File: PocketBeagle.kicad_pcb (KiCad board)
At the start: 4 copper layers, 55 x 35 mm, 32 parts, among them J1 Conn_01x08_Male, J10 Conn_01x04_Male, J11 Conn_01x04_Male, J12 Conn_01x04_Male, J13 Conn_01x04_Male, J14 Conn_01x04_Male, J15 Conn_01x04_Male, J16 Conn_01x04_Male, J17 Conn_01x02_Male, J18 Conn_01x02_Male, J19 Conn_01x01_Male, J2 Conn_01x04_Male, J20 Conn_01x01_Male, J21 Conn_01x04_Male, J22 Conn_01x04_Male, J23 Conn_01x02_Male, J24 Conn_01x02_Male, J25 Conn_01x01_Male, J26 Conn_01x01_Male, J27 Conn_01x04_Male, J28 Conn_01x04_Male, J29 Conn_01x01_Male, J3 Conn_01x04_Male, J30 Conn_01x01_Male, J31 Conn_01x01_Male, J32 Conn_01x01_Male, J4 Conn_01x08_Male, J5 Conn_01x04_Male, J6 Conn_01x04_Male, J7 Conn_01x04_Male, J8 Conn_01x04_Male, J9 Conn_01x04_Male

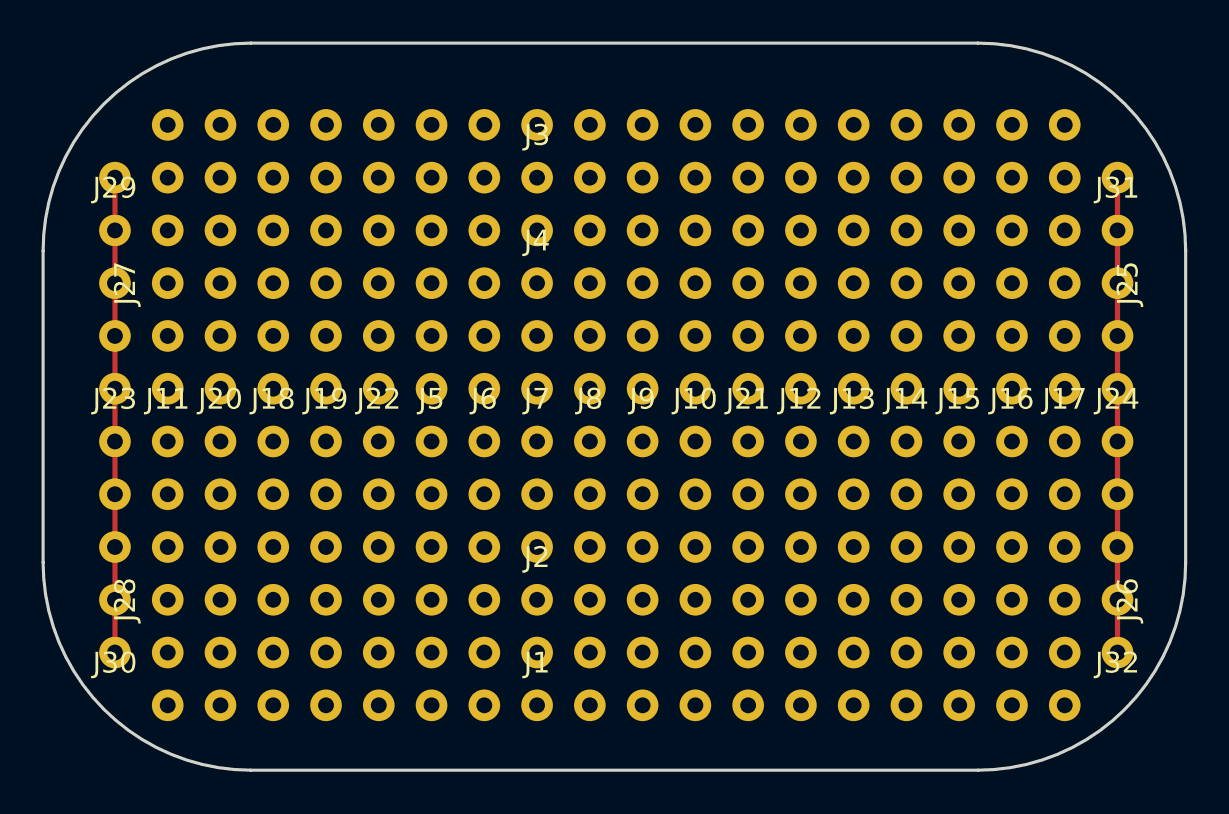
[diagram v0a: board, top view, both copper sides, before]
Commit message: Correct misalignment and delete unnecessary files. 位置ずれの修正と、不要なファイルの削除。
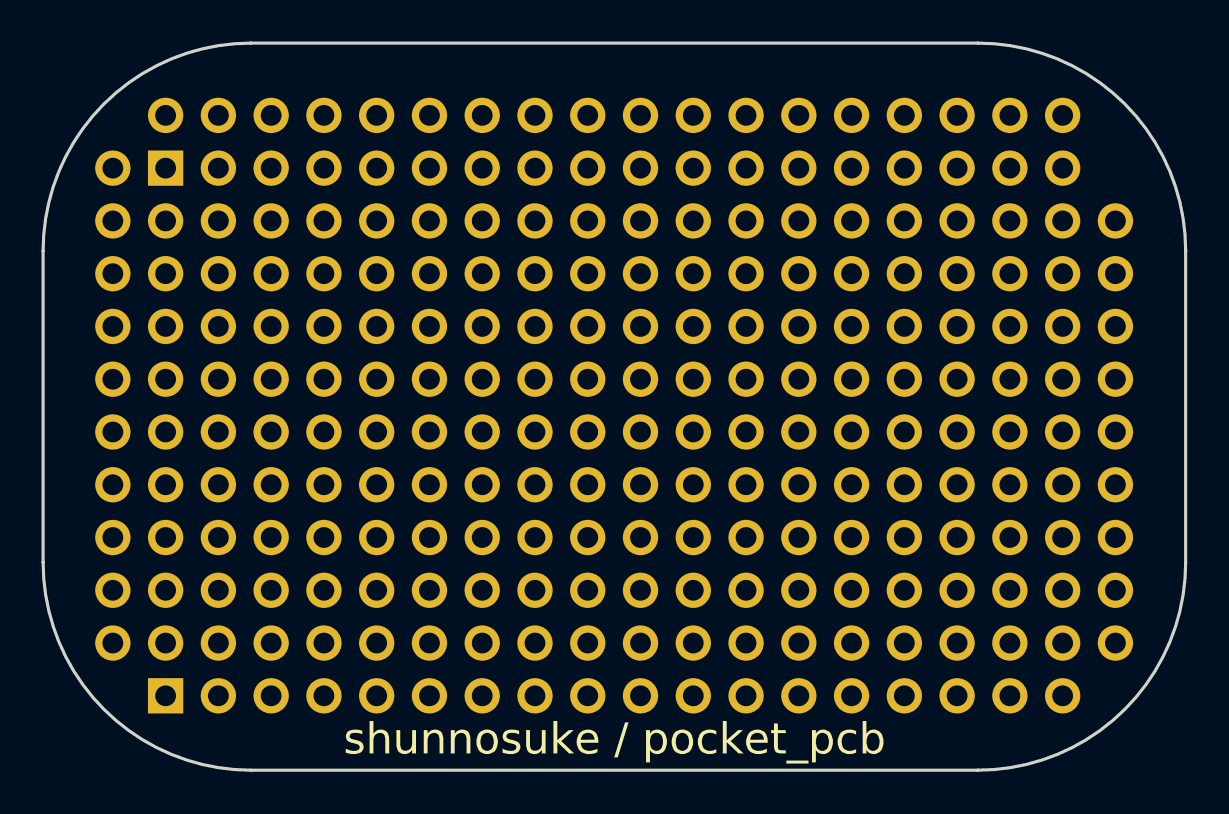
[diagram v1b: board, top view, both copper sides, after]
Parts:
- removed J25, J26: Conn_01x01_Male, pocketbeagle:j 2
- removed J27, J28: Conn_01x04_Male, pocketbeagle:j 2
- removed J29, J30, J31, J32: Conn_01x01_Male, pocketbeagle:j 1
- J1, J4: value Conn_01x08_Male -> Conn_01x18_Male; footprint pocketbeagle:端子 -> Connector_PinHeader_2.54mm:PinHeader_1x18_P2.54mm_Vertical
- J10, J11, J12, J13, J14, J15, J16, J21, J22, J7, J8, J9: value Conn_01x04_Male -> Conn_01x08_Male; footprint pocketbeagle:yb -> Connector_PinHeader_2.54mm:PinHeader_1x08_P2.54mm_Vertical
- J17, J18, J23, J24: value Conn_01x02_Male -> Conn_01x08_Male; footprint pocketbeagle:yb -> Connector_PinHeader_2.54mm:PinHeader_1x08_P2.54mm_Vertical
- J19, J20: value Conn_01x01_Male -> Conn_01x08_Male; footprint pocketbeagle:yb -> Connector_PinHeader_2.54mm:PinHeader_1x08_P2.54mm_Vertical
- J2, J3: value Conn_01x04_Male -> Conn_01x18_Male; footprint pocketbeagle:端子 -> Connector_PinHeader_2.54mm:PinHeader_1x18_P2.54mm_Vertical
- J5, J6: value Conn_01x04_Male -> Conn_01x10_Male; footprint pocketbeagle:yb -> Connector_PinHeader_2.54mm:PinHeader_1x10_P2.54mm_Vertical
- moved J23 43.8 mm to (167.5, 96.1)
- moved J6 32.2 mm to (172.6, 93.5)
- moved J20 31.4 mm to (159.9, 96.1)
- moved J22 29.0 mm to (165.0, 96.1)
- moved J18 24.1 mm to (154.8, 96.1)
- moved J19 24.1 mm to (157.4, 96.1)
- moved J13 19.6 mm to (142.1, 96.1)
- moved J17 19.6 mm to (152.3, 96.1)
- moved J9 19.6 mm to (132.0, 96.1)
- moved J7 19.6 mm to (126.9, 96.1)
- moved J10 19.6 mm to (134.5, 96.1)
- moved J12 19.6 mm to (139.6, 96.1)
- moved J14 19.6 mm to (144.7, 96.1)
- moved J15 19.6 mm to (147.2, 96.1)
- moved J16 19.6 mm to (149.8, 96.1)
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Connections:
- J1 pad 10: (no net) -> Net-(J1-Pad10)
- J1 pad 11: (no net) -> Net-(J1-Pad11)
- J1 pad 12: (no net) -> Net-(J1-Pad12)
- J1 pad 13: (no net) -> Net-(J1-Pad13)
- J1 pad 14: (no net) -> Net-(J1-Pad14)
- J1 pad 15: (no net) -> Net-(J1-Pad15)
- J1 pad 16: (no net) -> Net-(J1-Pad16)
- J1 pad 17: (no net) -> Net-(J1-Pad17)
- J1 pad 18: (no net) -> Net-(J1-Pad18)
- J1 pad 9: (no net) -> Net-(J1-Pad9)
- J16 pad 2: Net-(J16-Pad1) -> Net-(J16-Pad2)
- J16 pad 3: Net-(J16-Pad1) -> Net-(J16-Pad3)
- J16 pad 4: Net-(J16-Pad1) -> Net-(J16-Pad4)
- J17 pad 1: Net-(J16-Pad1) -> Net-(J17-Pad1)
- J17 pad 2: Net-(J16-Pad1) -> Net-(J17-Pad2)
- J17 pad 3: (no net) -> Net-(J17-Pad3)
- J17 pad 4: (no net) -> Net-(J17-Pad4)
- J18 pad 1: Net-(J16-Pad1) -> Net-(J18-Pad1)
- J18 pad 2: Net-(J16-Pad1) -> Net-(J18-Pad2)
- J18 pad 3: (no net) -> Net-(J18-Pad3)
- J18 pad 4: (no net) -> Net-(J18-Pad4)
- J19 pad 1: Net-(J16-Pad1) -> Net-(J19-Pad1)
- J19 pad 2: (no net) -> Net-(J19-Pad2)
- J19 pad 3: (no net) -> Net-(J19-Pad3)
- J19 pad 4: (no net) -> Net-(J19-Pad4)
- J2 pad 10: (no net) -> Net-(J2-Pad10)
- J2 pad 11: (no net) -> Net-(J2-Pad11)
- J2 pad 12: (no net) -> Net-(J2-Pad12)
- J2 pad 13: (no net) -> Net-(J2-Pad13)
- J2 pad 14: (no net) -> Net-(J2-Pad14)
- J2 pad 15: (no net) -> Net-(J2-Pad15)
- J2 pad 16: (no net) -> Net-(J2-Pad16)
- J2 pad 17: (no net) -> Net-(J2-Pad17)
- J2 pad 18: (no net) -> Net-(J2-Pad18)
- J2 pad 5: (no net) -> Net-(J2-Pad5)
- J2 pad 6: (no net) -> Net-(J2-Pad6)
- J2 pad 7: (no net) -> Net-(J2-Pad7)
- J2 pad 8: (no net) -> Net-(J2-Pad8)
- J2 pad 9: (no net) -> Net-(J2-Pad9)
- J20 pad 1: Net-(J16-Pad1) -> Net-(J20-Pad1)
- J20 pad 2: (no net) -> Net-(J20-Pad2)
- J20 pad 3: (no net) -> Net-(J20-Pad3)
- J20 pad 4: (no net) -> Net-(J20-Pad4)
- J22 pad 2: Net-(J22-Pad1) -> Net-(J22-Pad2)
- J22 pad 3: Net-(J22-Pad1) -> Net-(J22-Pad3)
- J22 pad 4: Net-(J22-Pad1) -> Net-(J22-Pad4)
- J23 pad 1: Net-(J22-Pad1) -> Net-(J23-Pad1)
- J23 pad 2: Net-(J22-Pad1) -> Net-(J23-Pad2)
- J23 pad 3: (no net) -> Net-(J23-Pad3)
- J23 pad 4: (no net) -> Net-(J23-Pad4)
- J24 pad 1: Net-(J22-Pad1) -> Net-(J24-Pad1)
- J24 pad 2: Net-(J22-Pad1) -> Net-(J24-Pad2)
- J24 pad 3: (no net) -> Net-(J24-Pad3)
- J24 pad 4: (no net) -> Net-(J24-Pad4)
- J3 pad 11: (no net) -> Net-(J3-Pad11)
- J3 pad 13: (no net) -> Net-(J3-Pad13)
- J3 pad 15: (no net) -> Net-(J3-Pad15)
- J3 pad 17: (no net) -> Net-(J3-Pad17)
- J3 pad 5: (no net) -> Net-(J3-Pad5)
- J3 pad 7: (no net) -> Net-(J3-Pad7)
- J3 pad 9: (no net) -> Net-(J3-Pad9)
- J4 pad 10: (no net) -> Net-(J4-Pad10)
- J4 pad 11: (no net) -> Net-(J4-Pad11)
- J4 pad 12: (no net) -> Net-(J4-Pad12)
- J4 pad 13: (no net) -> Net-(J4-Pad13)
- J4 pad 14: (no net) -> Net-(J4-Pad14)
- J4 pad 15: (no net) -> Net-(J4-Pad15)
- J4 pad 16: (no net) -> Net-(J4-Pad16)
- J4 pad 17: (no net) -> Net-(J4-Pad17)
- J4 pad 18: (no net) -> Net-(J4-Pad18)
- J4 pad 9: (no net) -> Net-(J4-Pad9)
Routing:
- net Net-(J24-Pad1): track 22.9 -> 0.00 mm
- net Net-(J23-Pad1): track 22.9 -> 0.00 mm
- removed copper zone on DigitalGND, net GND
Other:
- board text added: "75 Mils back--> Try to move back 75 Mils <---"
- board text added: "FillOverPAD:CGND:19:484"
- board text added: "FillOverPAD:CGND:19:532"
- board text added: "FillOverPAD:CGND:459:484"
- board text added: "FillOverPAD:CGND:460:484"
- board text added: "FillOverPAD:CGND:461:484"
- board text added: "FillOverPAD:CGND:462:484"
- board text added: "FillOverPAD:CGND:463:484"
- board text added: "FillOverPAD:CGND:464:484"
- board text added: "FillOverPAD:CGND:479:484"
- board text added: "FillOverPAD:CGND:480:484"
- board text added: "FillOverPAD:CGND:481:484"
- board text added: "FillOverPAD:CGND:482:484"
- board text added: "FillOverPAD:CGND:507:532"
- board text added: "FillOverPAD:CGND:508:532"
- board text added: "FillOverPAD:CGND:509:532"
- board text added: "FillOverPAD:CGND:510:532"
- board text added: "FillOverPAD:CGND:511:532"
- board text added: "FillOverPAD:CGND:512:532"
- board text added: "FillOverPAD:CGND:527:532"
- board text added: "FillOverPAD:CGND:528:532"
- board text added: "FillOverPAD:CGND:529:532"
- board text added: "FillOverPAD:CGND:530:532"
- board text added: "FillOverPAD:GND:102:484"
- board text added: "FillOverPAD:GND:102:532"
- board text added: "FillOverPAD:GND:106:484"
- board text added: "FillOverPAD:GND:106:532"
- board text added: "FillOverPAD:GND:10:484"
- board text added: "FillOverPAD:GND:10:532"
- board text added: "FillOverPAD:GND:112:484"
- board text added: "FillOverPAD:GND:112:532"
- board text added: "FillOverPAD:GND:113:484"
- board text added: "FillOverPAD:GND:113:532"
- board text added: "FillOverPAD:GND:114:484"
- board text added: "FillOverPAD:GND:114:532"
- board text added: "FillOverPAD:GND:115:484"
- board text added: "FillOverPAD:GND:115:532"
- board text added: "FillOverPAD:GND:120:484"
- board text added: "FillOverPAD:GND:120:532"
- board text added: "FillOverPAD:GND:123:484"
- board text added: "FillOverPAD:GND:123:532"
- board text added: "FillOverPAD:GND:128:484"
- board text added: "FillOverPAD:GND:128:532"
- board text added: "FillOverPAD:GND:129:484"
- board text added: "FillOverPAD:GND:129:532"
- board text added: "FillOverPAD:GND:12:484"
- board text added: "FillOverPAD:GND:12:532"
- board text added: "FillOverPAD:GND:131:484"
- board text added: "FillOverPAD:GND:131:532"
- board text added: "FillOverPAD:GND:136:484"
- board text added: "FillOverPAD:GND:136:532"
- board text added: "FillOverPAD:GND:137:484"
- board text added: "FillOverPAD:GND:137:532"
- board text added: "FillOverPAD:GND:138:484"
- board text added: "FillOverPAD:GND:138:532"
- board text added: "FillOverPAD:GND:139:484"
- board text added: "FillOverPAD:GND:139:532"
- board text added: "FillOverPAD:GND:145:484"
- board text added: "FillOverPAD:GND:145:532"
- board text added: "FillOverPAD:GND:146:484"
- board text added: "FillOverPAD:GND:146:532"
- board text added: "FillOverPAD:GND:147:484"
- board text added: "FillOverPAD:GND:147:532"
- board text added: "FillOverPAD:GND:148:484"
- board text added: "FillOverPAD:GND:148:532"
- board text added: "FillOverPAD:GND:149:484"
- board text added: "FillOverPAD:GND:149:532"
- board text added: "FillOverPAD:GND:150:484"
- board text added: "FillOverPAD:GND:150:532"
- board text added: "FillOverPAD:GND:172:484"
- board text added: "FillOverPAD:GND:172:532"
- board text added: "FillOverPAD:GND:20:484"
- board text added: "FillOverPAD:GND:20:532"
- board text added: "FillOverPAD:GND:238:484"
- board text added: "FillOverPAD:GND:238:532"
- board text added: "FillOverPAD:GND:239:484"
- board text added: "FillOverPAD:GND:239:532"
- board text added: "FillOverPAD:GND:251:484"
- board text added: "FillOverPAD:GND:251:532"
- board text added: "FillOverPAD:GND:252:484"
- board text added: "FillOverPAD:GND:252:532"
- board text added: "FillOverPAD:GND:253:484"
- board text added: "FillOverPAD:GND:253:532"
- board text added: "FillOverPAD:GND:254:484"
- board text added: "FillOverPAD:GND:254:532"
- board text added: "FillOverPAD:GND:255:484"
- board text added: "FillOverPAD:GND:255:532"
- board text added: "FillOverPAD:GND:256:484"
- board text added: "FillOverPAD:GND:256:532"
- board text added: "FillOverPAD:GND:257:484"
- board text added: "FillOverPAD:GND:257:532"
- board text added: "FillOverPAD:GND:258:484"
- board text added: "FillOverPAD:GND:258:532"
- board text added: "FillOverPAD:GND:267:484"
- board text added: "FillOverPAD:GND:267:532"
- board text added: "FillOverPAD:GND:274:484"
- board text added: "FillOverPAD:GND:274:532"
- board text added: "FillOverPAD:GND:283:484"
- board text added: "FillOverPAD:GND:283:532"
- board text added: "FillOverPAD:GND:290:484"
- board text added: "FillOverPAD:GND:290:532"
- board text added: "FillOverPAD:GND:298:484"
- board text added: "FillOverPAD:GND:298:532"
- board text added: "FillOverPAD:GND:299:484"
- board text added: "FillOverPAD:GND:299:532"
- board text added: "FillOverPAD:GND:2:484"
- board text added: "FillOverPAD:GND:2:532"
- board text added: "FillOverPAD:GND:306:484"
- board text added: "FillOverPAD:GND:306:532"
- board text added: "FillOverPAD:GND:307:484"
- board text added: "FillOverPAD:GND:307:532"
- board text added: "FillOverPAD:GND:314:484"
- board text added: "FillOverPAD:GND:314:532"
- board text added: "FillOverPAD:GND:315:484"
- board text added: "FillOverPAD:GND:315:532"
- board text added: "FillOverPAD:GND:322:484"
- board text added: "FillOverPAD:GND:322:532"
- board text added: "FillOverPAD:GND:323:484"
- board text added: "FillOverPAD:GND:323:532"
- board text added: "FillOverPAD:GND:331:484"
- board text added: "FillOverPAD:GND:331:532"
- board text added: "FillOverPAD:GND:338:484"
- board text added: "FillOverPAD:GND:338:532"
- board text added: "FillOverPAD:GND:347:484"
- board text added: "FillOverPAD:GND:347:532"
- board text added: "FillOverPAD:GND:354:484"
- board text added: "FillOverPAD:GND:354:532"
- board text added: "FillOverPAD:GND:363:484"
- board text added: "FillOverPAD:GND:363:532"
- board text added: "FillOverPAD:GND:364:484"
- board text added: "FillOverPAD:GND:364:532"
- board text added: "FillOverPAD:GND:365:484"
- board text added: "FillOverPAD:GND:365:532"
- board text added: "FillOverPAD:GND:366:484"
- board text added: "FillOverPAD:GND:366:532"
- board text added: "FillOverPAD:GND:367:484"
- board text added: "FillOverPAD:GND:367:532"
- board text added: "FillOverPAD:GND:368:484"
- board text added: "FillOverPAD:GND:368:532"
- board text added: "FillOverPAD:GND:369:484"
- board text added: "FillOverPAD:GND:369:532"
- board text added: "FillOverPAD:GND:370:484"
- board text added: "FillOverPAD:GND:370:532"
- board text added: "FillOverPAD:GND:382:484"
- board text added: "FillOverPAD:GND:382:532"
- board text added: "FillOverPAD:GND:383:484"
- board text added: "FillOverPAD:GND:383:532"
- board text added: "FillOverPAD:GND:441:484"
- board text added: "FillOverPAD:GND:441:532"
- board text added: "FillOverPAD:GND:447:484"
- board text added: "FillOverPAD:GND:447:532"
- board text added: "FillOverPAD:GND:467:484"
- board text added: "FillOverPAD:GND:475:484"
- board text added: "FillOverPAD:GND:515:532"
- board text added: "FillOverPAD:GND:523:532"
- board text added: "FillOverPAD:GND:8:484"
- board text added: "FillOverPAD:GND:8:532"
- board text added: "FillOverPAD:GND:96:484"
- board text added: "FillOverPAD:GND:96:532"
- board text added: "FillOverPAD:GND:97:484"
- board text added: "FillOverPAD:GND:97:532"
- board text added: "FillOverPAD:SYS_5V:332:484"
- board text added: "FillOverPAD:SYS_5V:332:532"
- board text added: "FillOverPAD:SYS_5V:333:484"
- board text added: "FillOverPAD:SYS_5V:333:532"
- board text added: "FillOverPAD:SYS_5V:348:484"
- board text added: "FillOverPAD:SYS_5V:348:532"
- board text added: "FillOverPAD:SYS_5V:349:484"
- board text added: "FillOverPAD:SYS_5V:349:532"
- board text added: "FillOverPAD:USB_DC:18:484"
- board text added: "FillOverPAD:USB_DC:18:532"
- board text added: "FillOverPAD:USB_DC:326:484"
- board text added: "FillOverPAD:USB_DC:326:532"
- board text added: "FillOverPAD:USB_DC:399:484"
- board text added: "FillOverPAD:USB_DC:399:532"
- board text added: "FillOverPAD:USB_DC:415:484"
- board text added: "FillOverPAD:USB_DC:415:532"
- board text added: "FillOverPAD:USB_DC:431:484"
- board text added: "FillOverPAD:USB_DC:431:532"
- board text added: "FillOverPAD:USB_DC:449:484"
- board text added: "FillOverPAD:USB_DC:449:532"
- board text added: "FillOverPAD:USB_DC:7:484"
- board text added: "FillOverPAD:USB_DC:7:532"
- board text added: "FillOverPAD:VBUS.RAW:17:484"
- board text added: "FillOverPAD:VBUS.RAW:17:532"
- board text added: "FillOverPAD:VBUS.RAW:469:484"
- board text added: "FillOverPAD:VBUS.RAW:517:532"
- board text added: "FillOverPAD:VDD_1V8:272:484"
- board text added: "FillOverPAD:VDD_1V8:272:532"
- board text added: "FillOverPAD:VDD_1V8:288:484"
- board text added: "FillOverPAD:VDD_1V8:288:532"
- board text added: "FillOverPAD:VDD_1V8:304:484"
- board text added: "FillOverPAD:VDD_1V8:304:532"
- board text added: "FillOverPAD:VDD_1V8:305:484"
- board text added: "FillOverPAD:VDD_1V8:305:532"
- board text added: "FillOverPAD:VDD_1V8:320:484"
- board text added: "FillOverPAD:VDD_1V8:320:532"
- board text added: "FillOverPAD:VDD_1V8:321:484"
- board text added: "FillOverPAD:VDD_1V8:321:532"
- board text added: "FillOverPAD:VDD_1V8:336:484"
- board text added: "FillOverPAD:VDD_1V8:336:532"
- board text added: "FillOverPAD:VDD_1V8:352:484"
- board text added: "FillOverPAD:VDD_1V8:352:532"
- board text added: "FillOverPAD:VDD_3V3A:270:484"
- board text added: "FillOverPAD:VDD_3V3A:270:532"
- board text added: "FillOverPAD:VDD_3V3A:271:484"
- board text added: "FillOverPAD:VDD_3V3A:271:532"
- board text added: "FillOverPAD:VDD_3V3A:286:484"
- board text added: "FillOverPAD:VDD_3V3A:286:532"
- board text added: "FillOverPAD:VDD_3V3A:287:484"
- board text added: "FillOverPAD:VDD_3V3A:287:532"
- board text added: "FillOverPAD:VDD_3V3A:301:484"
- board text added: "FillOverPAD:VDD_3V3A:301:532"
- board text added: "FillOverPAD:VDD_3V3A:302:484"
- board text added: "FillOverPAD:VDD_3V3A:302:532"
- board text added: "FillOverPAD:VDD_3V3A:303:484"
- board text added: "FillOverPAD:VDD_3V3A:303:532"
- board text added: "FillOverPAD:VDD_3V3A:317:484"
- board text added: "FillOverPAD:VDD_3V3A:317:532"
- board text added: "FillOverPAD:VDD_3V3A:318:484"
- board text added: "FillOverPAD:VDD_3V3A:318:532"
- board text added: "FillOverPAD:VDD_3V3A:319:484"
- board text added: "FillOverPAD:VDD_3V3A:319:532"
- board text added: "FillOverPAD:VDD_3V3A:334:484"
- board text added: "FillOverPAD:VDD_3V3A:334:532"
- board text added: "FillOverPAD:VDD_3V3A:335:484"
- board text added: "FillOverPAD:VDD_3V3A:335:532"
- board text added: "FillOverPAD:VDD_3V3A:350:484"
- board text added: "FillOverPAD:VDD_3V3A:350:532"
- board text added: "FillOverPAD:VDD_3V3A:351:484"
- board text added: "FillOverPAD:VDD_3V3A:351:532"
- board text added: "FillOverPAD:VDD_3V3AUX:100:484"
- board text added: "FillOverPAD:VDD_3V3AUX:100:532"
- board text added: "FillOverPAD:VDD_3V3AUX:273:484"
- board text added: "FillOverPAD:VDD_3V3AUX:273:532"
- board text added: "FillOverPAD:VDD_3V3AUX:289:484"
- board text added: "FillOverPAD:VDD_3V3AUX:289:532"
- board text added: "FillOverPAD:VDD_3V3B:11:484"
- board text added: "FillOverPAD:VDD_3V3B:11:532"
- board text added: "FillOverPAD:VDD_3V3B:130:484"
- board text added: "FillOverPAD:VDD_3V3B:130:532"
- board text added: "FillOverPAD:VDD_3V3B:144:484"
- board text added: "FillOverPAD:VDD_3V3B:144:532"
- board text added: "FillOverPAD:VDD_3V3B:151:484"
- board text added: "FillOverPAD:VDD_3V3B:151:532"
- board text added: "FillOverPAD:VDD_3V3B:160:484"
- board text added: "FillOverPAD:VDD_3V3B:160:532"
- board text added: "FillOverPAD:VDD_3V3B:161:484"
- board text added: "FillOverPAD:VDD_3V3B:161:532"
- board text added: "FillOverPAD:VDD_3V3B:162:484"
- board text added: "FillOverPAD:VDD_3V3B:162:532"
- board text added: "FillOverPAD:VDD_3V3B:163:484"
- board text added: "FillOverPAD:VDD_3V3B:163:532"
- board text added: "FillOverPAD:VDD_3V3B:165:484"
- board text added: "FillOverPAD:VDD_3V3B:165:532"
- board text added: "FillOverPAD:VDD_3V3B:166:484"
- board text added: "FillOverPAD:VDD_3V3B:166:532"
- board text added: "FillOverPAD:VDD_3V3B:167:484"
- board text added: "FillOverPAD:VDD_3V3B:167:532"
- board text added: "FillOverPAD:VDD_3V3B:268:484"
- board text added: "FillOverPAD:VDD_3V3B:268:532"
- board text added: "FillOverPAD:VDD_3V3B:269:484"
- board text added: "FillOverPAD:VDD_3V3B:269:532"
- board text added: "FillOverPAD:VDD_3V3B:284:484"
- board text added: "FillOverPAD:VDD_3V3B:284:532"
- board text added: "FillOverPAD:VDD_3V3B:285:484"
- board text added: "FillOverPAD:VDD_3V3B:285:532"
- board text added: "FillOverPAD:VDD_3V3B:473:484"
- board text added: "FillOverPAD:VDD_3V3B:521:532"
- board text added: "FillOverPAD:VDD_3V3B:9:484"
- board text added: "FillOverPAD:VDD_3V3B:9:532"
- board text added: "FillOverPAD:VDD_5V:400:484"
- board text added: "FillOverPAD:VDD_5V:400:532"
- board text added: "FillOverPAD:VDD_5V:416:484"
- board text added: "FillOverPAD:VDD_5V:416:532"
- board text added: "FillOverPAD:VDD_5V:432:484"
- board text added: "FillOverPAD:VDD_5V:432:532"
- board text added: "FillOverPAD:VDD_RTC:1:484"
- board text added: "FillOverPAD:VDD_RTC:1:532"
- board text added: "FillOverPAD:VDD_RTC:337:484"
- board text added: "FillOverPAD:VDD_RTC:337:532"
- board text added: "FillOverPAD:VDD_RTC:353:484"
- board text added: "FillOverPAD:VDD_RTC:353:532"
- board text added: "FillOverPAD:VDD_RTC:443:484"
- board text added: "FillOverPAD:VDD_RTC:443:532"
- board text added: "FillOverPAD:VIN.BAT:381:484"
- board text added: "FillOverPAD:VIN.BAT:381:532"
- board text added: "FillOverPAD:VIN.BAT:398:484"
- board text added: "FillOverPAD:VIN.BAT:398:532"
- board text added: "FillOverPAD:VIN.BAT:414:484"
- board text added: "FillOverPAD:VIN.BAT:414:532"
- board text added: "FillOverPAD:VIN.BAT:430:484"
- board text added: "FillOverPAD:VIN.BAT:430:532"
- board text added: "TE:CGND:1:28::L19"
- board text added: "TE:GND:2:28::L19"
- board text added: "TE:GND:3:28::L19"
- board text added: "TE:GND:4:28::L19"
- board text added: "TE:VDD_3V3AUX:1:8::L2"
- board text added: "TE:VDD_3V3AUX:2:8::L2"
- board text added: "TE:VDD_3V3AUX:3:8::L2"
- board text added: "TE:VDD_3V3AUX:5:28::L19"
- board text added: "TE:VDD_3V3AUX:6:28::L19"
- board text added: "TE:VDD_3V3AUX:7:28::L19"
- board text added: "TE:VDD_3V3AUX:8:28::L19"
- board text added: "TE:VDD_3V3B:10:28::L19"
- board text added: "TE:VDD_3V3B:11:28::L19"
- board text added: "TE:VDD_3V3B:12:28::L19"
- board text added: "TE:VDD_3V3B:13:28::L19"
- board text added: "TE:VDD_3V3B:14:28::L19"
- board text added: "TE:VDD_3V3B:15:28::L19"
- board text added: "TE:VDD_3V3B:16:28::L19"
- board text added: "TE:VDD_3V3B:17:28::L19"
- board text added: "TE:VDD_3V3B:18:28::L19"
- board text added: "TE:VDD_3V3B:19:28::L19"
- board text added: "TE:VDD_3V3B:20:28::L19"
- board text added: "TE:VDD_3V3B:21:28::L19"
- board text added: "TE:VDD_3V3B:22:28::L19"
- board text added: "TE:VDD_3V3B:23:28::L19"
- board text added: "TE:VDD_3V3B:24:28::L19"
- board text added: "TE:VDD_3V3B:9:28::L19"
- board text added: "TE:VDD_RTC:25:28::L19"
- board text added: "TE:VDD_RTC:26:28::L19"
- board text added: "TE:VDD_RTC:27:28::L19"
- board text added: "TE:VDD_RTC:28:28::L19"
- board text added: "TE:VDD_RTC:4:8::L2"
- board text added: "TE:VDD_RTC:5:8::L2"
- board text added: "TE:VDD_RTC:6:8::L2"
- board text added: "TE:VDD_RTC:7:8::L2"
- board text added: "TE:VDD_RTC:8:8::L2"
- board text added: "TS:CGND:1:28::L19"
- board text added: "TS:GND:2:28::L19"
- board text added: "TS:GND:3:28::L19"
- board text added: "TS:GND:4:28::L19"
- board text added: "TS:VDD_3V3AUX:1:8::L2"
- board text added: "TS:VDD_3V3AUX:2:8::L2"
- board text added: "TS:VDD_3V3AUX:3:8::L2"
- board text added: "TS:VDD_3V3AUX:5:28::L19"
- board text added: "TS:VDD_3V3AUX:6:28::L19"
- board text added: "TS:VDD_3V3AUX:7:28::L19"
- board text added: "TS:VDD_3V3AUX:8:28::L19"
- board text added: "TS:VDD_3V3B:10:28::L19"
- board text added: "TS:VDD_3V3B:11:28::L19"
- board text added: "TS:VDD_3V3B:12:28::L19"
- board text added: "TS:VDD_3V3B:13:28::L19"
- board text added: "TS:VDD_3V3B:14:28::L19"
- board text added: "TS:VDD_3V3B:15:28::L19"
- board text added: "TS:VDD_3V3B:16:28::L19"
- board text added: "TS:VDD_3V3B:17:28::L19"
- board text added: "TS:VDD_3V3B:18:28::L19"
- board text added: "TS:VDD_3V3B:19:28::L19"
- board text added: "TS:VDD_3V3B:20:28::L19"
- board text added: "TS:VDD_3V3B:21:28::L19"
- board text added: "TS:VDD_3V3B:22:28::L19"
- board text added: "TS:VDD_3V3B:23:28::L19"
- board text added: "TS:VDD_3V3B:24:28::L19"
- board text added: "TS:VDD_3V3B:9:28::L19"
- board text added: "TS:VDD_RTC:25:28::L19"
- board text added: "TS:VDD_RTC:26:28::L19"
- board text added: "TS:VDD_RTC:27:28::L19"
- board text added: "TS:VDD_RTC:28:28::L19"
- board text added: "TS:VDD_RTC:4:8::L2"
- board text added: "TS:VDD_RTC:5:8::L2"
- board text added: "TS:VDD_RTC:6:8::L2"
- board text added: "TS:VDD_RTC:7:8::L2"
- board text added: "TS:VDD_RTC:8:8::L2"
- board text added: "V:CGND:10:48"
- board text added: "V:CGND:11:48"
- board text added: "V:CGND:12:48"
- board text added: "V:CGND:13:48"
- board text added: "V:CGND:14:48"
- board text added: "V:CGND:15:48"
- board text added: "V:CGND:16:48"
- board text added: "V:CGND:17:48"
- board text added: "V:CGND:18:48"
- board text added: "V:CGND:19:48"
- board text added: "V:CGND:1:48"
- board text added: "V:CGND:20:48"
- board text added: "V:CGND:21:48"
- board text added: "V:CGND:22:48"
- board text added: "V:CGND:23:48"
- board text added: "V:CGND:24:48"
- board text added: "V:CGND:25:48"
- board text added: "V:CGND:26:48"
- board text added: "V:CGND:27:48"
- board text added: "V:CGND:28:48"
- board text added: "V:CGND:29:48"
- board text added: "V:CGND:2:48"
- board text added: "V:CGND:30:48"
- board text added: "V:CGND:31:48"
- board text added: "V:CGND:32:48"
- board text added: "V:CGND:33:48"
- board text added: "V:CGND:34:48"
- board text added: "V:CGND:3:48"
- board text added: "V:CGND:4:48"
- board text added: "V:CGND:5:48"
- board text added: "V:CGND:6:48"
- board text added: "V:CGND:7:48"
- board text added: "V:CGND:8:48"
- board text added: "V:CGND:9:48"
- board text added: "V:GND:35:48"
- board text added: "V:GND:36:48"
- board text added: "V:GND:37:48"
- board text added: "V:GND:38:48"
- board text added: "V:GND:39:48"
- board text added: "V:GND:40:48"
- board text added: "V:GND:41:48"
- board text added: "V:GND:42:48"
- board text added: "V:GND:43:48"
- board text added: "V:GND:44:48"
- board text added: "V:VDD_3V3AUX:45:48"
- board text added: "V:VDD_3V3B:46:48"
- board text added: "V:VDD_3V3B:47:48"
- board text added: "V:VDD_RTC:48:48"
- board text added: "shunnosuke / pocket_pcb"
